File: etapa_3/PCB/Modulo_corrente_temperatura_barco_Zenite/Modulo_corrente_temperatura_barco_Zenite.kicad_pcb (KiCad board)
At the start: 2 copper layers, 60 x 150 mm, 11 parts, among them U2 LM7805, U3 TLV9004IDR, U4 MCP2515-xSO, U5 MCP2551-I-SN, Y1 16MHz

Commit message: PCB layout V1 added - DRC review nedded
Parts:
- added C1: 10uF, Capacitor_THT:CP_Radial_D6.3mm_P2.50mm, F.Cu at (84.9, 55.4)
- added C10: 22pF, Capacitor_SMD:C_0805_2012Metric_Pad1.18x1.45mm_HandSolder, B.Cu at (137.2, 57.6)
- added C11: 100nF, Capacitor_THT:C_Disc_D7.5mm_W2.5mm_P5.00mm, F.Cu at (131.5, 47.5)
- added C12: 100uF, Capacitor_THT:CP_Radial_D6.3mm_P2.50mm, F.Cu at (109.4, 64.3)
- added C13: 100uF, Capacitor_THT:CP_Radial_D6.3mm_P2.50mm, F.Cu at (108.1, 46.1)
- added C2: 470pF, Capacitor_SMD:C_0805_2012Metric_Pad1.18x1.45mm_HandSolder, B.Cu at (100.7, 49.7)
- added C3: 220nF, Capacitor_THT:C_Disc_D7.5mm_W2.5mm_P5.00mm, F.Cu at (84.1, 65.3)
- added C4: 100nF, Capacitor_THT:C_Disc_D7.5mm_W2.5mm_P5.00mm, F.Cu at (104.0, 69.7)
- added C5: 100nF, Capacitor_THT:C_Disc_D7.5mm_W2.5mm_P5.00mm, F.Cu at (104.0, 95.6)
- added C6: 470pF, Capacitor_SMD:C_0805_2012Metric_Pad1.18x1.45mm_HandSolder, B.Cu at (95.1, 84.7)
- added C7: 1nF, Capacitor_SMD:C_0805_2012Metric_Pad1.18x1.45mm_HandSolder, B.Cu at (88.7, 86.9)
- added C8: 100nF, Capacitor_THT:C_Disc_D7.5mm_W2.5mm_P5.00mm, F.Cu at (119.8, 74.9)
- added C9: 22pF, Capacitor_SMD:C_0805_2012Metric_Pad1.18x1.45mm_HandSolder, B.Cu at (133.4, 57.6)
- added D1: D, Diode_THT:D_5W_P10.16mm_Horizontal, F.Cu at (87.5, 35.6)
- added D2: D_Zener, Diode_THT:D_5W_P10.16mm_Horizontal, F.Cu at (87.5, 39.2)
- added D3: D_Zener, Diode_THT:D_5W_P10.16mm_Horizontal, F.Cu at (107.2, 69.9)
- added D4: D_Zener, Diode_THT:D_5W_P10.16mm_Horizontal, F.Cu at (105.3, 63.0)
- added D5: D_Zener, Diode_THT:D_5W_P10.16mm_Horizontal, F.Cu at (116.4, 46.1)
- added F1: Fuse, pi-III-lib:fuse_holder, F.Cu at (95.3, 41.6)
- added J1: RJ45_Shielded, Connector_RJ:RJ45_Ninigi_GE, F.Cu at (116.3, 38.0)
- added J2: RJ45_Shielded, Connector_RJ:RJ45_Ninigi_GE, F.Cu at (135.9, 38.1)
- added J3: Conn_01x03, pi-III-lib:B3BXHALFSN, F.Cu at (120.0, 58.6)
- added R1: 100k, Resistor_THT:R_Axial_DIN0207_L6.3mm_D2.5mm_P10.16mm_Horizontal, F.Cu at (92.4, 153.3)
- added R10: 100k, Resistor_SMD:R_0805_2012Metric_Pad1.20x1.40mm_HandSolder, B.Cu at (110.1, 84.8)
- added R11: 10k, Resistor_SMD:R_0805_2012Metric_Pad1.20x1.40mm_HandSolder, B.Cu at (97.4, 80.7)
- added R12: 4k7, Resistor_SMD:R_0805_2012Metric_Pad1.20x1.40mm_HandSolder, B.Cu at (92.8, 81.9)
- added R13: 4k7, Resistor_SMD:R_0805_2012Metric_Pad1.20x1.40mm_HandSolder, B.Cu at (138.9, 41.2)
- added R14: 33, Resistor_SMD:R_2010_5025Metric_Pad1.40x2.65mm_HandSolder, B.Cu at (112.3, 78.6)
- added R15: 0R, Resistor_SMD:R_0805_2012Metric_Pad1.20x1.40mm_HandSolder, B.Cu at (96.1, 101.2)
- added R2: 100k, Resistor_THT:R_Axial_DIN0207_L6.3mm_D2.5mm_P10.16mm_Horizontal, F.Cu at (97.4, 156.3)
- added R3: 100k, Resistor_THT:R_Axial_DIN0207_L6.3mm_D2.5mm_P10.16mm_Horizontal, F.Cu at (102.1, 159.3)
- added R4: 100k, Resistor_SMD:R_0805_2012Metric_Pad1.20x1.40mm_HandSolder, B.Cu at (98.6, 97.4)
- added R5: 100k, Resistor_SMD:R_0805_2012Metric_Pad1.20x1.40mm_HandSolder, B.Cu at (94.7, 97.4)
- added R6: 100k, Resistor_SMD:R_0805_2012Metric_Pad1.20x1.40mm_HandSolder, B.Cu at (90.7, 92.7)
- added R7: 100k, Resistor_SMD:R_0805_2012Metric_Pad1.20x1.40mm_HandSolder, B.Cu at (100.9, 84.2)
- added R8: 33, Resistor_SMD:R_2010_5025Metric_Pad1.40x2.65mm_HandSolder, B.Cu at (112.3, 75.2)
- added R9: 100k, Resistor_SMD:R_0805_2012Metric_Pad1.20x1.40mm_HandSolder, B.Cu at (106.6, 85.8)
- L1, U4, U5: moved to B.Cu
- U2: footprint Package_TO_SOT_THT:TO-220-3_Vertical -> Package_TO_SOT_THT:TO-220-3_Horizontal_TabDown
- U3: value TLV9004IDR -> TLV9004; moved to B.Cu
- moved MAX3 100.0 mm to (149.4, 91.7), turned to -90 degrees
- moved MAX1 86.8 mm to (149.4, 142.8), turned to -90 degrees
- moved MAX2 77.1 mm to (149.6, 117.2), turned to -90 degrees
- moved U3 62.4 mm to (97.9, 91.0), turned to 90 degrees
- moved U4 41.0 mm to (132.1, 68.1), turned to -90 degrees
- moved Y1 30.8 mm to (137.7, 60.2), turned to 180 degrees
- moved MIC1 29.2 mm to (95.9, 126.6), turned to 180 degrees
- moved L1 27.4 mm to (87.1, 60.3)
- moved PS1 21.8 mm to (92.8, 53.9)
- moved U2 19.2 mm to (101.2, 74.7), turned to 90 degrees
- moved U5 16.7 mm to (135.7, 46.7), turned to 90 degrees
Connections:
- MAX1 pad 2: Net-(MAX1-CS) -> A8
- MAX1 pad 3: MOSI3 -> MOSI2
- MAX1 pad 4: MISO3 -> MISO2
- MAX1 pad 5: SCK3 -> SCK2
- MAX2 pad 2: Net-(MAX2-CS) -> A9
- MAX2 pad 3: MOSI3 -> MOSI2
- MAX2 pad 4: MISO3 -> MISO2
- MAX2 pad 5: SCK3 -> SCK2
- MAX3 pad 2: Net-(MAX3-CS) -> A10
- MAX3 pad 3: MOSI3 -> MOSI2
- MAX3 pad 4: MISO3 -> MISO2
- MAX3 pad 5: SCK3 -> SCK2
- MIC1 pad 18: 5V -> unconnected-(MIC1-5V-Pad18)
- MIC1 pad 5: unconnected-(MIC1-A8-Pad5) -> A8
- MIC1 pad 6: unconnected-(MIC1-A9-Pad6) -> A9
- MIC1 pad 7: unconnected-(MIC1-A10-Pad7) -> A10
- U3 pad 1: Net-(U3A--) -> (no net)
- U3 pad 11: GND -> AGND
- U3 pad 2: Net-(U3A--) -> (no net)
- U3 pad 3: Net-(U3A-+) -> (no net)
- U3 pad 5: (no net) -> Net-(U3B-+)
- U3 pad 6: (no net) -> Net-(U3B--)
- U3 pad 7: (no net) -> Net-(U3B--)
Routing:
- net 5V: track 0.00 -> 149.5 mm
- net 3V3: track 0.00 -> 144.7 mm
- net MISO2: track 0.00 -> 135.3 mm
- net NSS2: track 0.00 -> 127.7 mm, vias 0 -> 2
- net MOSI2: track 0.00 -> 127.6 mm, vias 0 -> 2
- net SCK2: track 0.00 -> 116.8 mm
- net A10: track 0.00 -> 111.0 mm
- net A9: track 0.00 -> 73.1 mm
- net MISO3: track 68.9 -> 0.00 mm
- net SCK3: track 68.8 -> 0.00 mm
- net MOSI3: track 68.6 -> 0.00 mm
- net CAN_18V: track 0.00 -> 56.4 mm
- net CAN_18V_p: track 0.00 -> 55.0 mm
- net GND: track 0.00 -> 51.8 mm, vias 0 -> 17
- net I_signal: track 0.00 -> 43.5 mm, vias 0 -> 2
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- added copper zone on B.Cu, net AGND
- added copper zone on F.Cu, net AGND
- added copper zone on B.Cu, net GND
- added copper zone on F.Cu, net GND
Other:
- board size 60 x 150 mm -> 60 x 138.6 mm

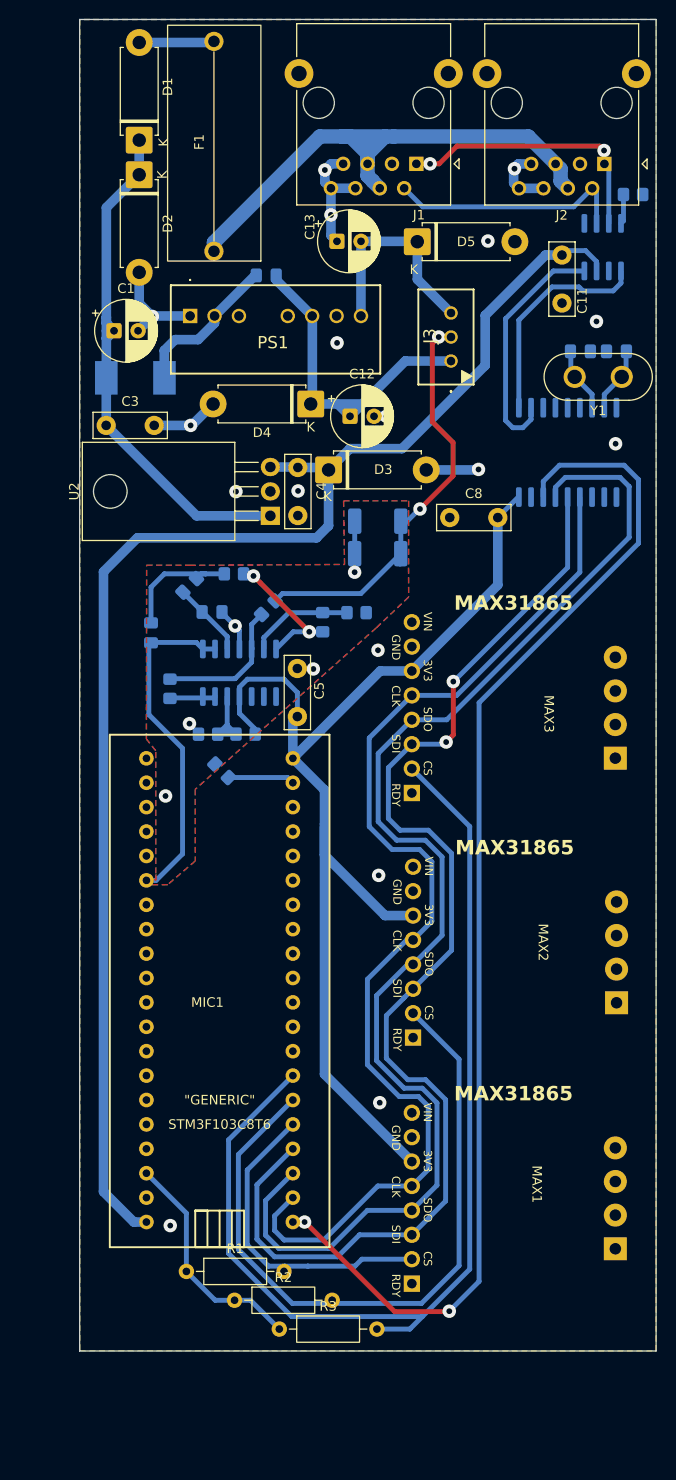
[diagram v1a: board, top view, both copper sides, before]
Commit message: Updated PCB version - DRC and final routing needed
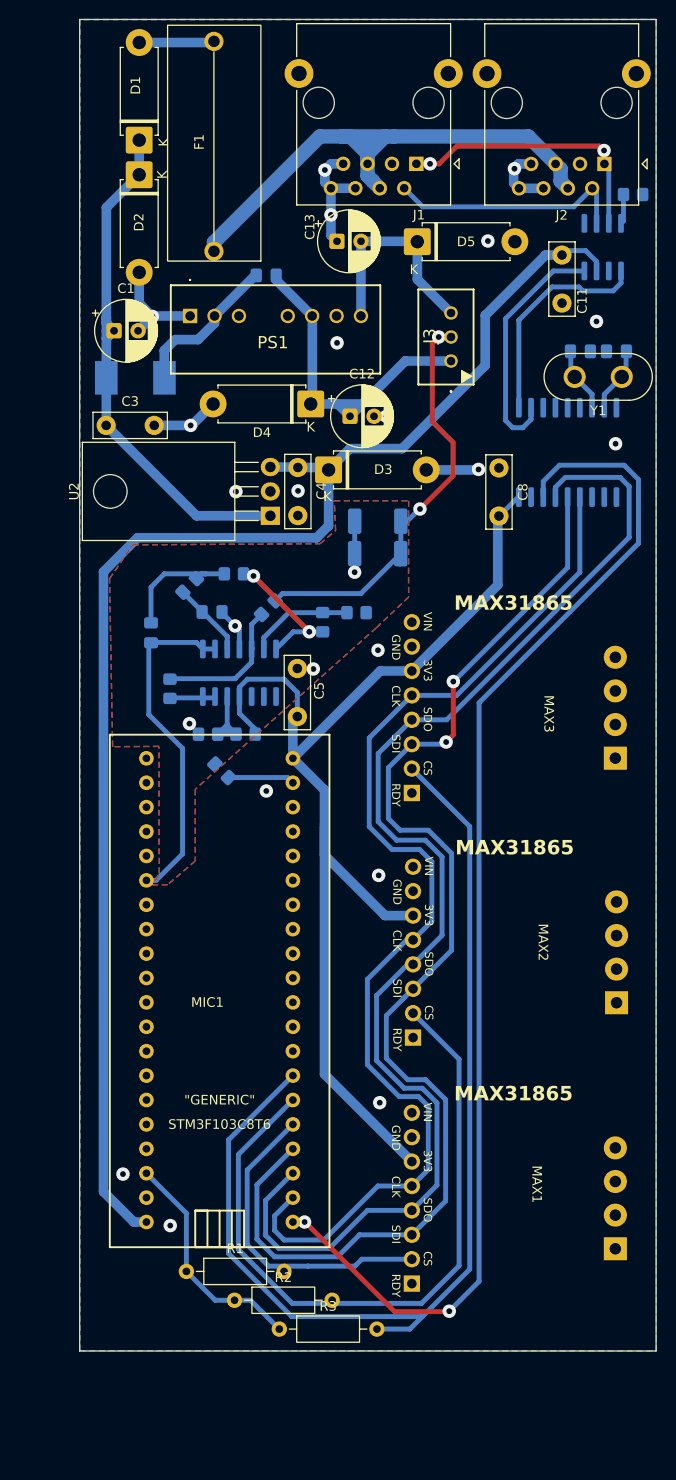
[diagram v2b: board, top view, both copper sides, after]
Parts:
- moved C8 7.27 mm to (124.9, 69.7), turned to -90 degrees
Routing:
- net GND: vias 17 -> 19
- net AGND: vias 5 -> 4
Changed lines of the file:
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@@
 		(tags "Diode 5W series Axial Horizontal pin pitch 10.16mm  length 8.9mm diameter 3.7mm")
 		(property "Reference" "D2"
-			(at 5.08 -2.970001 90)
+			(at 4.95 0.02 90)
 			(layer "F.SilkS")
 			(effects
@@
 		(tags "Diode 5W series Axial Horizontal pin pitch 10.16mm  length 8.9mm diameter 3.7mm")
 		(property "Reference" "D1"
-			(at 5.55 2.97 90)
+			(at 5.69 -0.37 90)
 			(layer "F.SilkS")
 			(effects
@@
 	(footprint "Capacitor_THT:C_Disc_D7.5mm_W2.5mm_P5.00mm"
 		(layer "F.Cu")
-		(at 119.82 74.86)
+		(at 124.94 69.7 -90)
 		(descr "C, Disc series, Radial, pin pitch=5.00mm, diameter*width=7.5*2.5mm^2, Capacitor, http://www.vishay.com/docs/28535/vy2series.pdf")
 		(tags "C Disc series Radial pin pitch 5.00mm diameter 7.5mm width 2.5mm Capacitor")
 		(property "Reference" "C8"
-			(at 2.5 -2.5 0)
+			(at 2.5 -2.5 90)
 			(layer "F.SilkS")
 			(effects
@@
 		)
 		(property "Value" "100nF"
-			(at 2.5 2.5 0)
+			(at 2.5 2.5 90)
 			(layer "F.Fab")
 			(effects
@@
 		)
 		(property "Datasheet" "~"
-			(at 0 0 0)
+			(at 0 0 90)
 			(layer "F.Fab")
 			(hide yes)
@@
 		)
 		(property "Description" "Unpolarized capacitor"
-			(at 0 0 0)
+			(at 0 0 90)
 			(layer "F.Fab")
 			(hide yes)
@@
 		(attr through_hole)
 		(fp_line
-			(start -1.37 -1.37)
-			(end 6.37 -1.37)
+			(start -1.37 1.37)
+			(end -1.37 -1.37)
 			(stroke
 				(width 0.12)
@@
 		)
 		(fp_line
-			(start -1.37 1.37)
-			(end -1.37 -1.37)
+			(start 6.37 1.37)
+			(end -1.37 1.37)
 			(stroke
 				(width 0.12)
@@
 		)
 		(fp_line
-			(start 6.37 -1.37)
-			(end 6.37 1.37)
+			(start -1.37 -1.37)
+			(end 6.37 -1.37)
 			(stroke
 				(width 0.12)
@@
 		)
 		(fp_line
-			(start 6.37 1.37)
-			(end -1.37 1.37)
+			(start 6.37 -1.37)
+			(end 6.37 1.37)
 			(stroke
 				(width 0.12)
@@
 			(layer "F.SilkS")
 		)
-		(fp_rect
-			(start -1.5 -1.5)
-			(end 6.5 1.5)
+		(fp_poly
+			(pts
+				(xy -1.5 -1.5) (xy 6.5 -1.5) (xy 6.5 1.5) (xy -1.5 1.5)
+			)
 			(stroke
 				(width 0.05)
@@
 			(layer "F.CrtYd")
 		)
-		(fp_rect
-			(start -1.25 -1.25)
-			(end 6.25 1.25)
+		(fp_poly
+			(pts
+				(xy -1.25 -1.25) (xy 6.25 -1.25) (xy 6.25 1.25) (xy -1.25 1.25)
+			)
 			(stroke
 				(width 0.1)
@@
 		)
 		(fp_text user "${REFERENCE}"
-			(at 2.5 0 0)
+			(at 2.5 0 90)
 			(layer "F.Fab")
 			(effects
@@
 		)
 		(pad "1" thru_hole circle
-			(at 0 0)
+			(at 0 0 270)
 			(size 2 2)
 			(drill 1)
@@
 		)
 		(pad "2" thru_hole circle
-			(at 5 0)
+			(at 5 0 270)
 			(size 2 2)
 			(drill 1)
@@
 	)
 	(via
+		(at 100.73 103.32)
+		(size 1.4)
+		(drill 0.6)
+		(layers "F.Cu" "B.Cu")
+		(free yes)
+		(net 9)
+	)
+	(via
 		(at 122.81 69.85)
 		(size 1.4)
@@
 	)
 	(via
+		(at 85.81 143.19)
+		(size 1.4)
+		(drill 0.6)
+		(layers "F.Cu" "B.Cu")
+		(free yes)
+		(net 9)
+	)
+	(via
 		(at 108.09 56.68)
 		(size 1.4)
@@
 	)
 	(via
-		(at 90.24 103.84)
-		(size 1.4)
-		(drill 0.6)
-		(layers "F.Cu" "B.Cu")
-		(free yes)
-		(net 86)
-	)
-	(via
 		(at 105.62 90.62)
 		(size 1.4)
@@
 		(polygon
 			(pts
-				(xy 89.22 99.13) (xy 88.25 97.919292) (xy 88.27 79.81) (xy 92.75 79.83) (xy 108.87 79.74) (xy 108.77 73.12)
-				(xy 115.54 73.12) (xy 115.53 80.08) (xy 115.541653 83.133031) (xy 112.16073 86.348876) (xy 93.330006 103.143406)
-				(xy 93.341191 110.593292) (xy 90.465677 113.066576) (xy 88.113302 113.080095) (xy 89.03 112.48)
-				(xy 89.25 112.62) (xy 89.23 111.89)
+				(xy 89.55 98.68) (xy 84.732475 98.702297) (xy 84.41 81.23) (xy 86.83 77.7) (xy 106.329452 77.588992)
+				(xy 107.940211 76.215136) (xy 107.799365 73.12) (xy 115.54 73.12) (xy 115.53 80.08) (xy 115.541653 83.133031)
+				(xy 112.16073 86.348876) (xy 93.330006 103.143406) (xy 93.341191 110.593292) (xy 90.465677 113.066576)
+				(xy 88.113302 113.080095) (xy 89.03 112.48) (xy 89.25 112.62) (xy 89.57 111.9)
 			)
 		)
